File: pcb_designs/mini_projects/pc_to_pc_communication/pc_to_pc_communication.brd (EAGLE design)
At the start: 67 x 48.2 mm, 14 parts, among them IC1 MAX232, IC2 74S51N, T1 SL100, T2 SL100, X1 DB 9 FEMALE

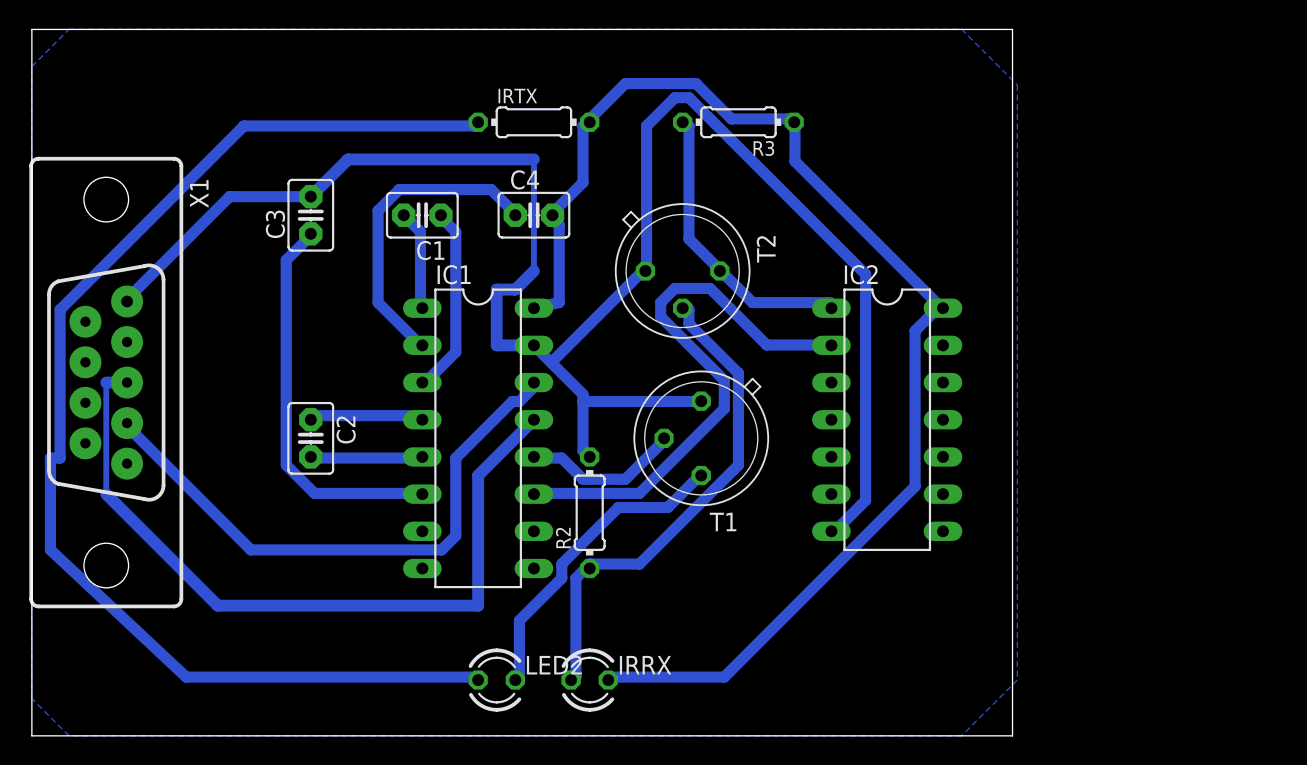
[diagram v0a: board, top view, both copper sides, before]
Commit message: 
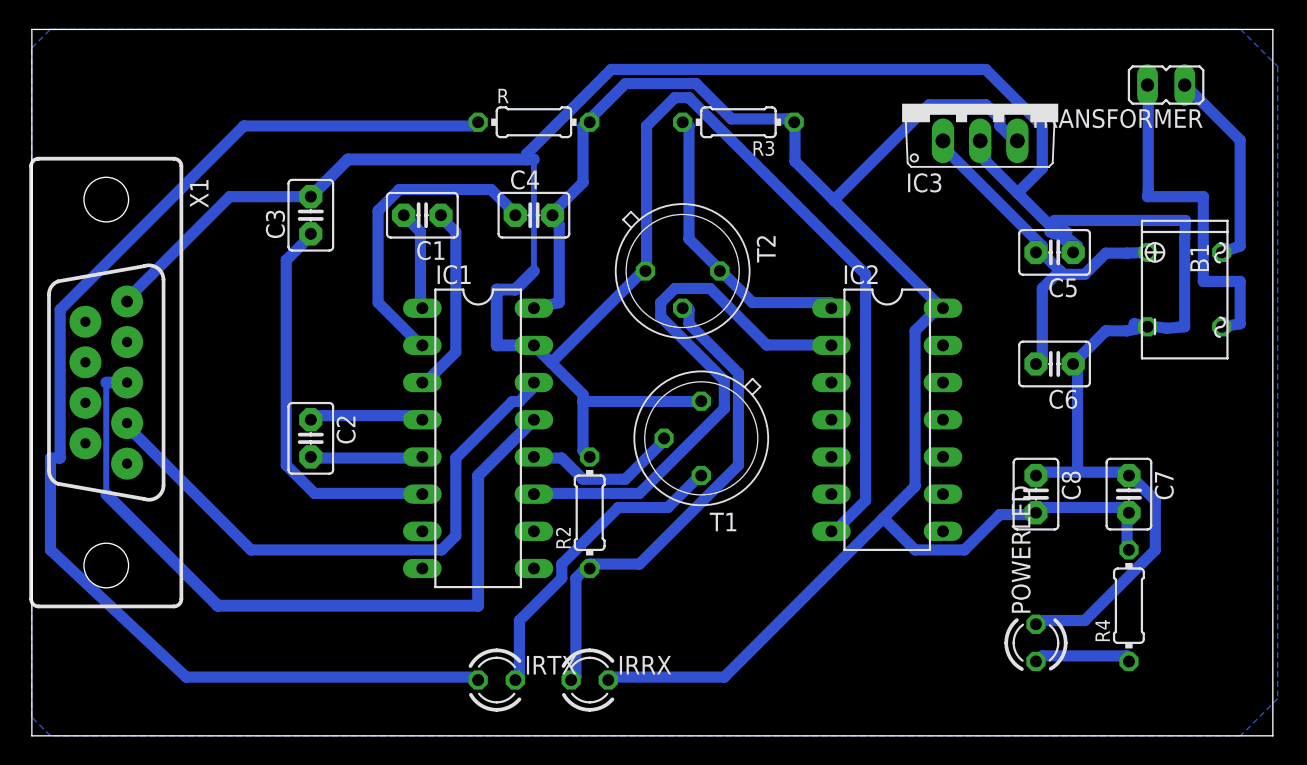
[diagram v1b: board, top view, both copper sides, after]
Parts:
- removed LED2: (no value), led:LED3MM
- added B1: (no value), rectifier:B-DIL
- added C5: 470uf, capacitor-wima:C2.5-3
- added C6, C8: 0.1uf, capacitor-wima:C2.5-3
- added C7: 4.7uf, capacitor-wima:C2.5-3
- added IC3: 7805TV, linear:TO220V
- added POWERLED: (no value), led:LED3MM
- added R, R4: 330R, resistor:0204/7
- added TRANSFORMER: (no value), jumper:JP1
- IRTX: value 330R -> (none); device resistor:0204/7 -> led:LED3MM
- moved IRTX 38.2 mm to (31.8, 15.2)
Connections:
- new net N$16: B1.+, C5.2, C6.2, IC3.1
- new net N$17: B1.AC1, TRANSFORMER.2
- new net N$18: B1.AC2, TRANSFORMER.1
- new net N$21: POWERLED.A, R4.1
- net +5V: now also C7.2, C8.2, IC3.3, R.2, R4.2; no longer IRTX.2
- net 0V: now also B1.-, C5.1, C6.1, C7.1, C8.1, IC3.2, POWERLED.K
- net N$6: now also IRTX.K; no longer LED2.K
- net N$8: now also IRTX.A, R.1; no longer IRTX.1, LED2.A
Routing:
- net 0V: track 124.5 -> 242.3 mm
- net +5V: track 88.5 -> 126.9 mm
- net N$16: track 0.00 -> 26.5 mm
- net N$17: track 0.00 -> 23.9 mm
- net N$18: track 0.00 -> 13.9 mm
- net N$21: track 0.00 -> 6.77 mm
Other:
- board size 67 x 48.2 mm -> 84.8 x 48.2 mm
